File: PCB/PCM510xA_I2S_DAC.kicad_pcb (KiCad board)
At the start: 2 copper layers, 40.6 x 25.5 mm, 35 parts, among them J1 EDGE_PINS, J2 TRS_LINE_OUT, U1 PCM5101A, U2 MIC5225-3.3

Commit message: update to 1.0.0
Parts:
- removed JP1: SCK, Jumper:SolderJumper-3_P1.3mm_Bridged12_RoundedPad1.0x1.5mm
- removed TP4: 3.3VA, TestPoint:TestPoint_Pad_2.0x2.0mm
- removed TP5: LDOO, TestPoint:TestPoint_Pad_2.0x2.0mm
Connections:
- U1 pad 12: /SCK -> GND
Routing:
- net /SCK: track 15.8 -> 0.00 mm, vias 1 -> 0
- net +3.3VA: track 36.2 -> 23.7 mm, vias 1 -> 0
- net +3.3V: track 36.9 -> 29.0 mm, vias 1 -> 0
- net /LDOO: track 16.4 -> 13.1 mm
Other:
- board text added: "2023-10-22 1.0.0"
- board text removed: "2023-10-02 0.0.2"
- board text removed: "HI"

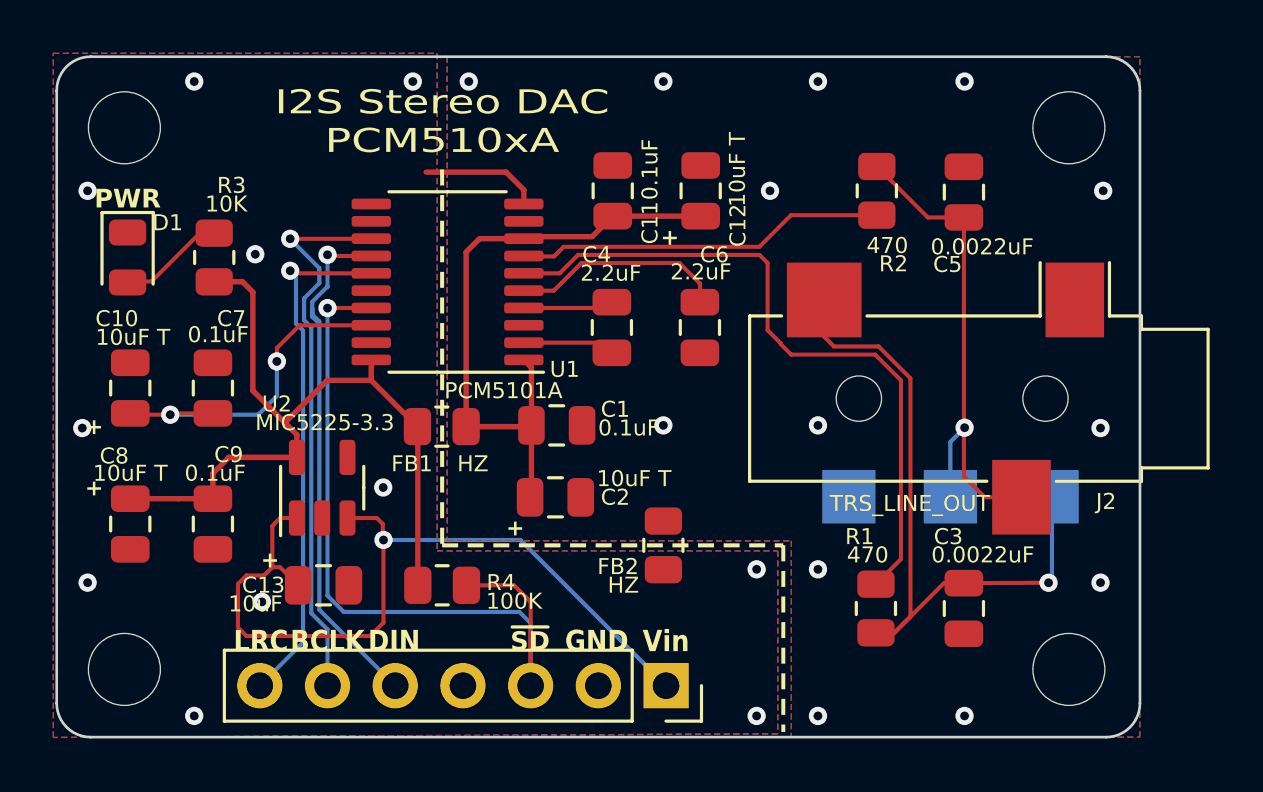
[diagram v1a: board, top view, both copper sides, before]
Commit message: update 3.3v regulator
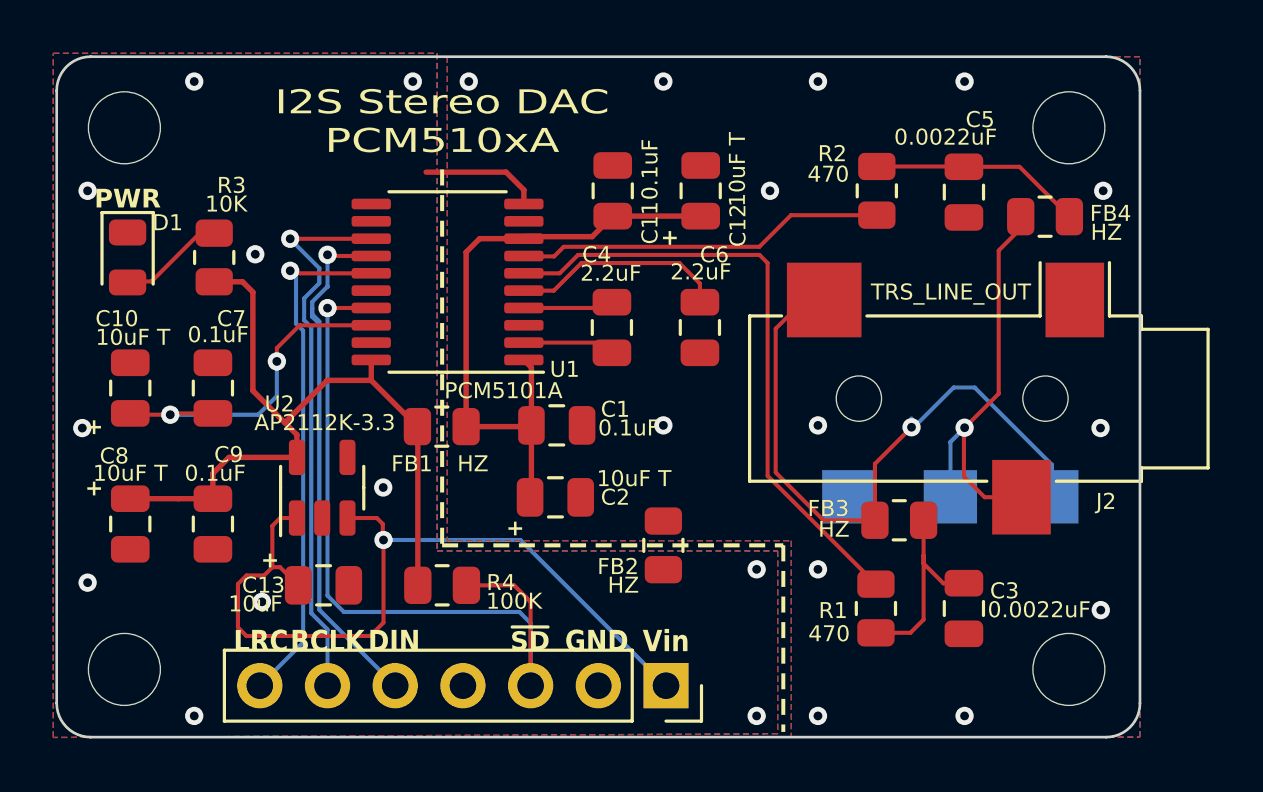
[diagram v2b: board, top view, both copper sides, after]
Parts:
- added FB3: HZ, Resistor_SMD:R_0805_2012Metric, F.Cu at (148.4, 108.5)
- added FB4: HZ, Resistor_SMD:R_0805_2012Metric, F.Cu at (153.9, 97.1)
- U2: value MIC5225-3.3 -> AP2112K-3.3
- turned C5 to -90 degrees
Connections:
- J2 pad R: Net-(C5-Pad1) -> Net-(FB4-Pad2)
- J2 pad T: Net-(C3-Pad1) -> Net-(FB3-Pad2)
- TP1 pad 1: Net-(C3-Pad1) -> Net-(FB3-Pad2)
- TP2 pad 1: Net-(C5-Pad1) -> Net-(FB4-Pad2)
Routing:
- net Net-(FB3-Pad2): track 0.00 -> 24.8 mm, vias 0 -> 1
- net Net-(C3-Pad1): track 25.5 -> 8.55 mm, vias 1 -> 0
- net Net-(FB4-Pad2): track 0.00 -> 16.0 mm, vias 0 -> 1
- net Net-(C5-Pad1): track 19.1 -> 8.00 mm, vias 1 -> 0
- net /OUTL: track 25.9 -> 23.3 mm
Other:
- board text added: "2023-11-22 1.0.1"
- board text removed: "2023-10-22 1.0.0"
- board text removed: "LO"
